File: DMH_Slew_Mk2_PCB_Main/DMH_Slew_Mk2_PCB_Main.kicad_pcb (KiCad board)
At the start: 2 copper layers, 48 x 175 mm, 33 parts, among them J0 Conn_01x01, J1 TS_Jack_6.35mm_Sw, J10 TS_Jack_6.35mm_Sw, J100 IDC_02x08, J14 Conn_02x03_Top_Bottom, J15 Conn_02x06_Top_Bottom, J16 Conn_02x03_Top_Bottom, J17 Conn_01x08, J18 Conn_01x08, J2 TS_Jack_6.35mm_Sw, J200 IDC_02x05, J24 Conn_02x03_Top_Bottom, J25 Conn_02x06_Top_Bottom, J26 Conn_02x03_Top_Bottom, J27 Conn_01x08, J28 Conn_01x08, J3 TS_Jack_6.35mm_Sw, J4 TS_Jack_6.35mm_Sw, J5 TS_Jack_6.35mm_Sw, J6 TS_Jack_6.35mm_Sw, J7 TS_Jack_6.35mm_Sw, J8 TS_Jack_6.35mm_Sw, J9 TS_Jack_6.35mm_Sw, U10 LM4040LP-10

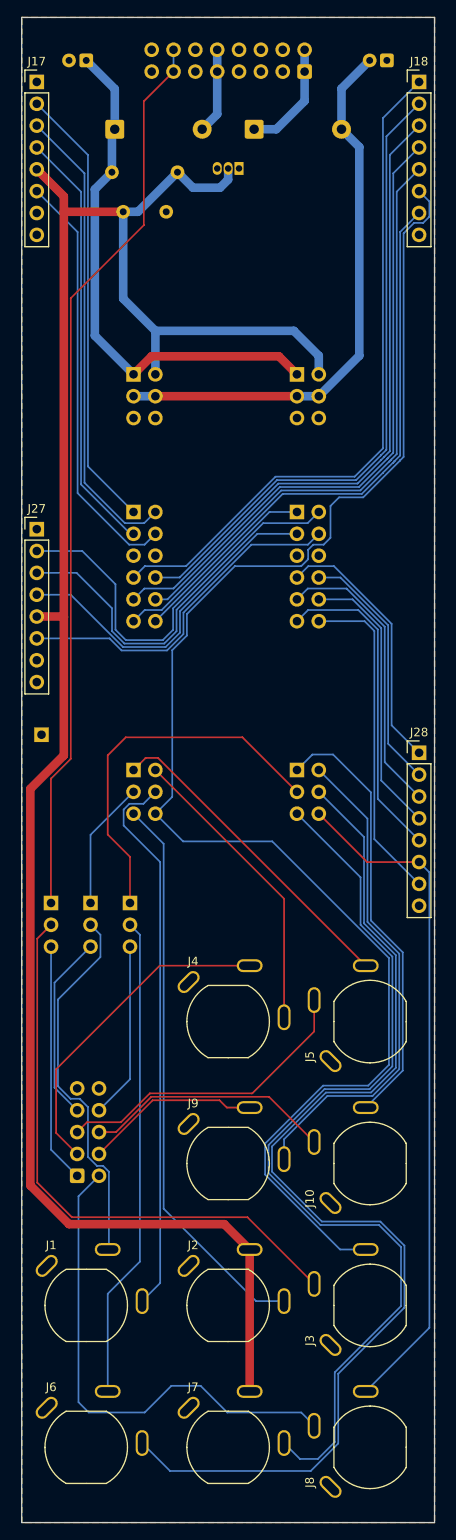
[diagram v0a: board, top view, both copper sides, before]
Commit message: Corrected gate outs and CV dest switch locations in PCBs
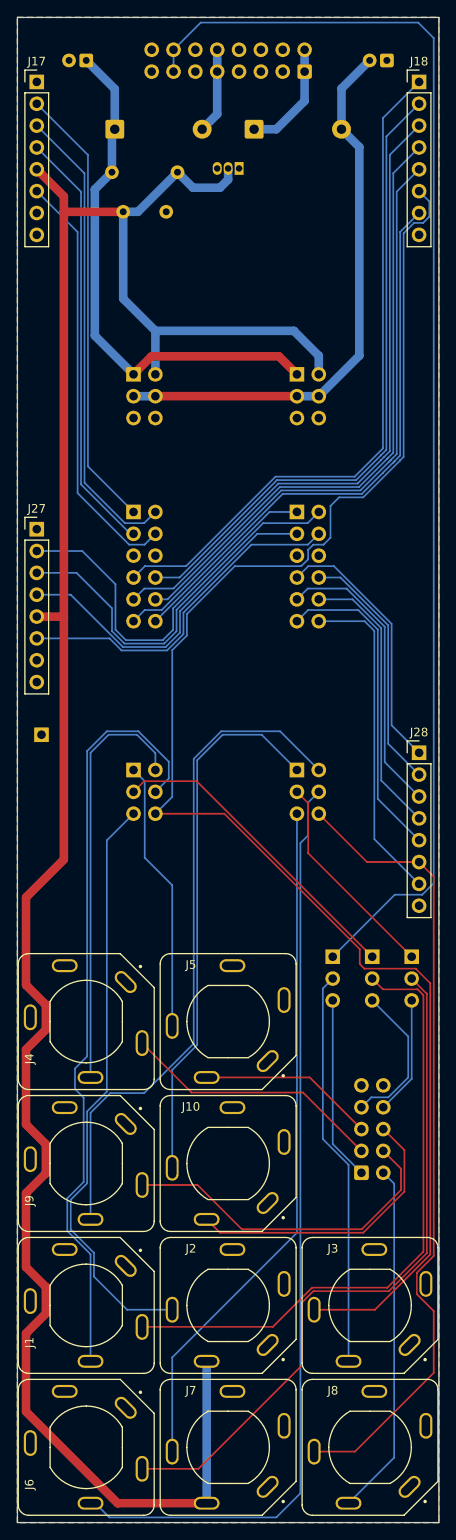
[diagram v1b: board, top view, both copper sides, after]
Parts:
- J1, J10, J2, J3, J4, J5, J6, J7, J8, J9: footprint SynthStuff:CUI_MJ-63052A -> SynthStuff:CUI_SJ-63083D
- moved JP1 33.3 mm to (87.2, 151.7)
- moved JP2 33.3 mm to (91.8, 151.7)
- moved JP3 33.3 mm to (96.3, 151.7)
- moved J200 33.1 mm to (90.5, 176.8)
- moved J10 16.5 mm to (75.0, 175.8), turned to 0 degrees
- moved J4 16.5 mm to (58.5, 159.2), turned to 90 degrees
- moved J5 16.5 mm to (75.0, 159.2), turned to 0 degrees
- moved J9 16.5 mm to (58.5, 175.8), turned to 90 degrees
- turned J1 to 90 degrees
- turned J3 to 0 degrees
- turned J6 to 90 degrees
- turned J8 to 0 degrees
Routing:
- net Bus_CV_M: track 105.1 -> 148.4 mm
- net A_In_Jack_TN_M: track 43.8 -> 72.9 mm
- net +10V: track 235.6 -> 264.6 mm
- net B_CV_In_Jack_M: track 107.7 -> 80.2 mm
- net A_Input_Jack_M: track 64.3 -> 89.9 mm
- net B_In_Jack_TN_M: track 56.3 -> 80.4 mm
- net A_Loopback_M: track 15.0 -> 36.7 mm
- net A_Out_Jack_TN_M: track 67.7 -> 46.2 mm
- net B_R_Gate_Jack_M: track 57.8 -> 78.6 mm
- net B_R_Gate_Jack_TN_M: track 20.4 -> 39.5 mm
- net B_Loopback_M: track 43.7 -> 24.7 mm
- net B_Input_Jack_M: track 127.5 -> 108.7 mm
- net B_Out_Jack_TN_M: track 58.4 -> 41.1 mm
- net A_F_Gate_Jack_TN_M: track 36.0 -> 20.5 mm
- net B_Out_Jack_M: track 79.1 -> 93.4 mm
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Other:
- board size 48 x 175 mm -> 49 x 175 mm
- board text added: "Mk2.1 - July 2026"
- board text removed: "Mk2.0 - April 2026"
